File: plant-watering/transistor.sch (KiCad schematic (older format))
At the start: 12 parts, among them Q1 BC337, Q2 BC337, Q3 BC337, Q4 BC337, Q5 BC337, Q6 BC337

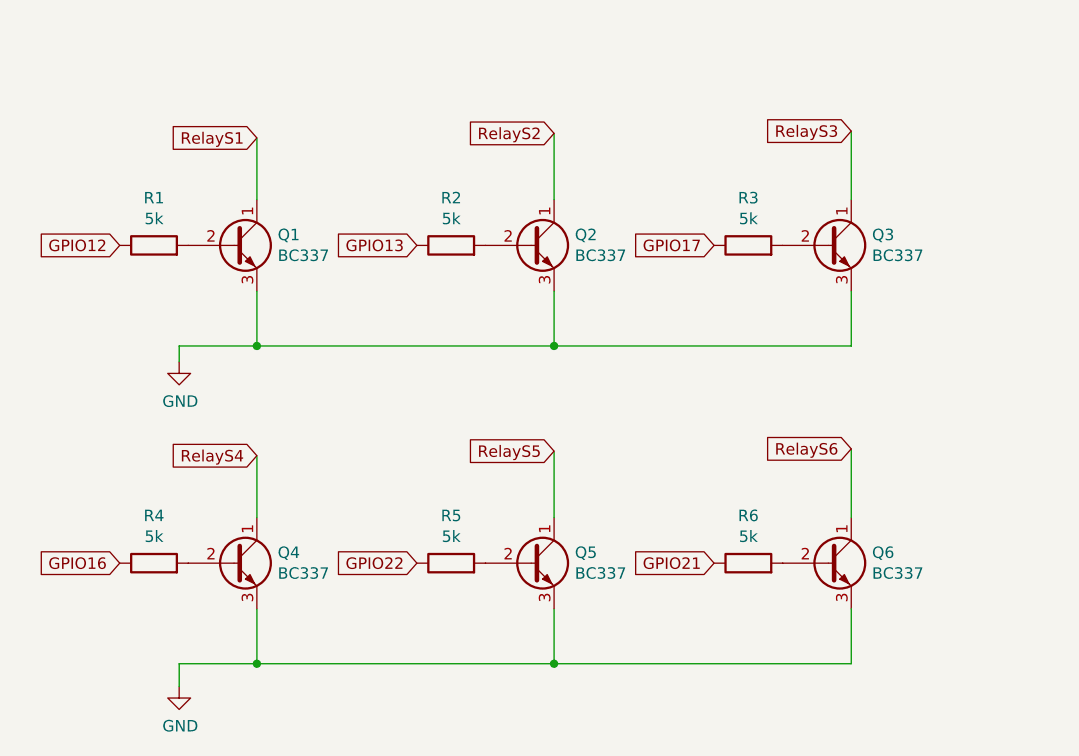
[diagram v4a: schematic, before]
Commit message: changed pcb parts
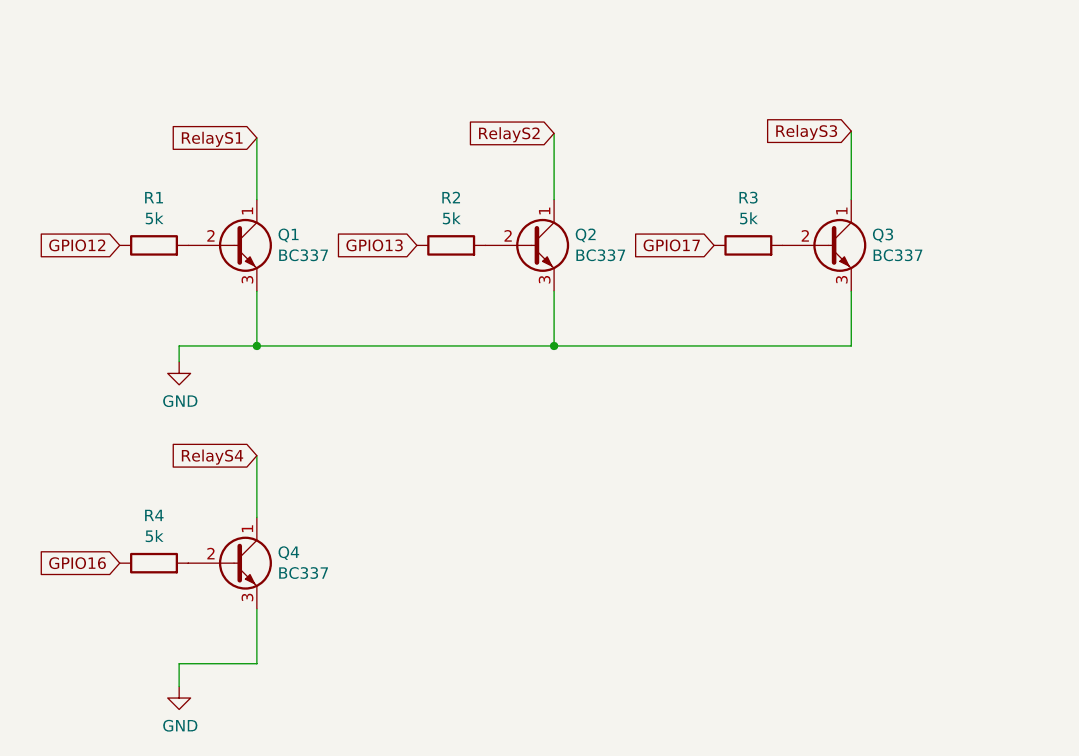
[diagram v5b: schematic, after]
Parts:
- removed Q5, Q6: BC337, TO_SOT_Packages_THT:TO-92_Inline_Wide, symbol Transistor_BJT:BC337
- removed R5, R6: 5k, Resistors_ThroughHole:R_Axial_DIN0207_L6.3mm_D2.5mm_P5.08mm_Vertical, symbol Device:R
- Q1, Q2, Q3, Q4: footprint TO_SOT_Packages_THT:TO-92_Inline_Wide -> Package_TO_SOT_THT:TO-92_Inline_Wide
- R1, R2, R3, R4: footprint Resistors_ThroughHole:R_Axial_DIN0207_L6.3mm_D2.5mm_P5.08mm_Vertical -> Resistor_THT:R_Axial_DIN0207_L6.3mm_D2.5mm_P5.08mm_Vertical
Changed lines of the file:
@@
 F 0 "Q2" H 5791 3616 50  0000 L CNN
 F 1 "BC337" H 5791 3525 50  0000 L CNN
-F 2 "TO_SOT_Packages_THT:TO-92_Inline_Wide" H 5800 3495 50  0001 L CIN
+F 2 "Package_TO_SOT_THT:TO-92_Inline_Wide" H 5800 3495 50  0001 L CIN
 F 3 "https://diotec.com/tl_files/diotec/files/pdf/datasheets/bc337.pdf" H 5600 3570 50  0001 L CNN
 	1    5600 3570
@@
 F 0 "Q1" H 4491 3616 50  0000 L CNN
 F 1 "BC337" H 4491 3525 50  0000 L CNN
-F 2 "TO_SOT_Packages_THT:TO-92_Inline_Wide" H 4500 3495 50  0001 L CIN
+F 2 "Package_TO_SOT_THT:TO-92_Inline_Wide" H 4500 3495 50  0001 L CIN
 F 3 "https://diotec.com/tl_files/diotec/files/pdf/datasheets/bc337.pdf" H 4300 3570 50  0001 L CNN
 	1    4300 3570
@@
 F 0 "Q3" H 7091 3616 50  0000 L CNN
 F 1 "BC337" H 7091 3525 50  0000 L CNN
-F 2 "TO_SOT_Packages_THT:TO-92_Inline_Wide" H 7100 3495 50  0001 L CIN
+F 2 "Package_TO_SOT_THT:TO-92_Inline_Wide" H 7100 3495 50  0001 L CIN
 F 3 "https://diotec.com/tl_files/diotec/files/pdf/datasheets/bc337.pdf" H 6900 3570 50  0001 L CNN
 	1    6900 3570
@@
 F 0 "R1" V 4157 3570 50  0000 C CNN
 F 1 "5k" V 4066 3570 50  0000 C CNN
-F 2 "Resistors_ThroughHole:R_Axial_DIN0207_L6.3mm_D2.5mm_P5.08mm_Vertical" V 3880 3570 50  0001 C CNN
+F 2 "Resistor_THT:R_Axial_DIN0207_L6.3mm_D2.5mm_P5.08mm_Vertical" V 3880 3570 50  0001 C CNN
 F 3 "~" H 3950 3570 50  0001 C CNN
 	1    3950 3570
@@
 F 0 "R2" V 5457 3570 50  0000 C CNN
 F 1 "5k" V 5366 3570 50  0000 C CNN
-F 2 "Resistors_ThroughHole:R_Axial_DIN0207_L6.3mm_D2.5mm_P5.08mm_Vertical" V 5180 3570 50  0001 C CNN
+F 2 "Resistor_THT:R_Axial_DIN0207_L6.3mm_D2.5mm_P5.08mm_Vertical" V 5180 3570 50  0001 C CNN
 F 3 "~" H 5250 3570 50  0001 C CNN
 	1    5250 3570
@@
 F 0 "R3" V 6757 3570 50  0000 C CNN
 F 1 "5k" V 6666 3570 50  0000 C CNN
-F 2 "Resistors_ThroughHole:R_Axial_DIN0207_L6.3mm_D2.5mm_P5.08mm_Vertical" V 6480 3570 50  0001 C CNN
+F 2 "Resistor_THT:R_Axial_DIN0207_L6.3mm_D2.5mm_P5.08mm_Vertical" V 6480 3570 50  0001 C CNN
 F 3 "~" H 6550 3570 50  0001 C CNN
 	1    6550 3570
@@
 	7000 3070 7000 3370
 $Comp
-L Transistor_BJT:BC337 Q5
-U 1 1 600EAB81
-P 5600 4960
-F 0 "Q5" H 5791 5006 50  0000 L CNN
-F 1 "BC337" H 5791 4915 50  0000 L CNN
-F 2 "TO_SOT_Packages_THT:TO-92_Inline_Wide" H 5800 4885 50  0001 L CIN
-F 3 "https://diotec.com/tl_files/diotec/files/pdf/datasheets/bc337.pdf" H 5600 4960 50  0001 L CNN
-	1    5600 4960
-	1    0    0    -1
-$EndComp
-$Comp
 L Transistor_BJT:BC337 Q4
 U 1 1 600EAB87
@@
 F 0 "Q4" H 4491 5006 50  0000 L CNN
 F 1 "BC337" H 4491 4915 50  0000 L CNN
-F 2 "TO_SOT_Packages_THT:TO-92_Inline_Wide" H 4500 4885 50  0001 L CIN
+F 2 "Package_TO_SOT_THT:TO-92_Inline_Wide" H 4500 4885 50  0001 L CIN
 F 3 "https://diotec.com/tl_files/diotec/files/pdf/datasheets/bc337.pdf" H 4300 4960 50  0001 L CNN
 	1    4300 4960
-	1    0    0    -1
-$EndComp
-$Comp
-L Transistor_BJT:BC337 Q6
-U 1 1 600EAB8D
-P 6900 4960
-F 0 "Q6" H 7091 5006 50  0000 L CNN
-F 1 "BC337" H 7091 4915 50  0000 L CNN
-F 2 "TO_SOT_Packages_THT:TO-92_Inline_Wide" H 7100 4885 50  0001 L CIN
-F 3 "https://diotec.com/tl_files/diotec/files/pdf/datasheets/bc337.pdf" H 6900 4960 50  0001 L CNN
-	1    6900 4960
 	1    0    0    -1
 $EndComp
@@
 F 0 "R4" V 4157 4960 50  0000 C CNN
 F 1 "5k" V 4066 4960 50  0000 C CNN
-F 2 "Resistors_ThroughHole:R_Axial_DIN0207_L6.3mm_D2.5mm_P5.08mm_Vertical" V 3880 4960 50  0001 C CNN
+F 2 "Resistor_THT:R_Axial_DIN0207_L6.3mm_D2.5mm_P5.08mm_Vertical" V 3880 4960 50  0001 C CNN
 F 3 "~" H 3950 4960 50  0001 C CNN
 	1    3950 4960
 	0    -1   -1   0
 $EndComp
-$Comp
-L Device:R R5
-U 1 1 600EAB99
-P 5250 4960
-F 0 "R5" V 5457 4960 50  0000 C CNN
-F 1 "5k" V 5366 4960 50  0000 C CNN
-F 2 "Resistors_ThroughHole:R_Axial_DIN0207_L6.3mm_D2.5mm_P5.08mm_Vertical" V 5180 4960 50  0001 C CNN
-F 3 "~" H 5250 4960 50  0001 C CNN
-	1    5250 4960
-	0    -1   -1   0
-$EndComp
-$Comp
-L Device:R R6
-U 1 1 600EAB9F
-P 6550 4960
-F 0 "R6" V 6757 4960 50  0000 C CNN
-F 1 "5k" V 6666 4960 50  0000 C CNN
-F 2 "Resistors_ThroughHole:R_Axial_DIN0207_L6.3mm_D2.5mm_P5.08mm_Vertical" V 6480 4960 50  0001 C CNN
-F 3 "~" H 6550 4960 50  0001 C CNN
-	1    6550 4960
-	0    -1   -1   0
-$EndComp
 Text GLabel 4400 4490 0    50   Input ~ 0
 RelayS4
-Text GLabel 5700 4470 0    50   Input ~ 0
-RelayS5
-Text GLabel 7000 4460 0    50   Input ~ 0
-RelayS6
-Wire Wire Line
-	7000 5160 7000 5400
 Wire Wire Line
 	4400 5160 4400 5400
 Wire Wire Line
-	5700 5160 5700 5400
-Wire Wire Line
-	4400 5400 5700 5400
-Connection ~ 5700 5400
-Wire Wire Line
-	5700 5400 7000 5400
-Wire Wire Line
 	4400 4490 4400 4760
-Wire Wire Line
-	5700 4760 5700 4470
-Wire Wire Line
-	7000 4460 7000 4760
 Wire Wire Line
 	4400 5400 4060 5400
 Wire Wire Line
 	4060 5400 4060 5500
-Connection ~ 4400 5400
 $Comp
 L power:GND #PWR0108
@@
 Text GLabel 3800 4960 0    50   Input ~ 0
 GPIO16
-Text GLabel 5100 4960 0    50   Input ~ 0
-GPIO22
-Text GLabel 6400 4960 0    50   Input ~ 0
-GPIO21
 $EndSCHEMATC

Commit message: changed parts on pcb
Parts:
- R1, R2, R3, R4: footprint Resistor_THT:R_Axial_DIN0207_L6.3mm_D2.5mm_P5.08mm_Vertical -> Resistor_THT:R_Axial_DIN0207_L6.3mm_D2.5mm_P7.62mm_Horizontal
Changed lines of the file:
@@
 F 0 "R1" V 4157 3570 50  0000 C CNN
 F 1 "5k" V 4066 3570 50  0000 C CNN
-F 2 "Resistor_THT:R_Axial_DIN0207_L6.3mm_D2.5mm_P5.08mm_Vertical" V 3880 3570 50  0001 C CNN
+F 2 "Resistor_THT:R_Axial_DIN0207_L6.3mm_D2.5mm_P7.62mm_Horizontal" V 3880 3570 50  0001 C CNN
 F 3 "~" H 3950 3570 50  0001 C CNN
 	1    3950 3570
@@
 F 0 "R2" V 5457 3570 50  0000 C CNN
 F 1 "5k" V 5366 3570 50  0000 C CNN
-F 2 "Resistor_THT:R_Axial_DIN0207_L6.3mm_D2.5mm_P5.08mm_Vertical" V 5180 3570 50  0001 C CNN
+F 2 "Resistor_THT:R_Axial_DIN0207_L6.3mm_D2.5mm_P7.62mm_Horizontal" V 5180 3570 50  0001 C CNN
 F 3 "~" H 5250 3570 50  0001 C CNN
 	1    5250 3570
@@
 F 0 "R3" V 6757 3570 50  0000 C CNN
 F 1 "5k" V 6666 3570 50  0000 C CNN
-F 2 "Resistor_THT:R_Axial_DIN0207_L6.3mm_D2.5mm_P5.08mm_Vertical" V 6480 3570 50  0001 C CNN
+F 2 "Resistor_THT:R_Axial_DIN0207_L6.3mm_D2.5mm_P7.62mm_Horizontal" V 6480 3570 50  0001 C CNN
 F 3 "~" H 6550 3570 50  0001 C CNN
 	1    6550 3570
@@
 F 0 "R4" V 4157 4960 50  0000 C CNN
 F 1 "5k" V 4066 4960 50  0000 C CNN
-F 2 "Resistor_THT:R_Axial_DIN0207_L6.3mm_D2.5mm_P5.08mm_Vertical" V 3880 4960 50  0001 C CNN
+F 2 "Resistor_THT:R_Axial_DIN0207_L6.3mm_D2.5mm_P7.62mm_Horizontal" V 3880 4960 50  0001 C CNN
 F 3 "~" H 3950 4960 50  0001 C CNN
 	1    3950 4960
